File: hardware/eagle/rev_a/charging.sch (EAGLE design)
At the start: 25 parts, among them U1 LM2622

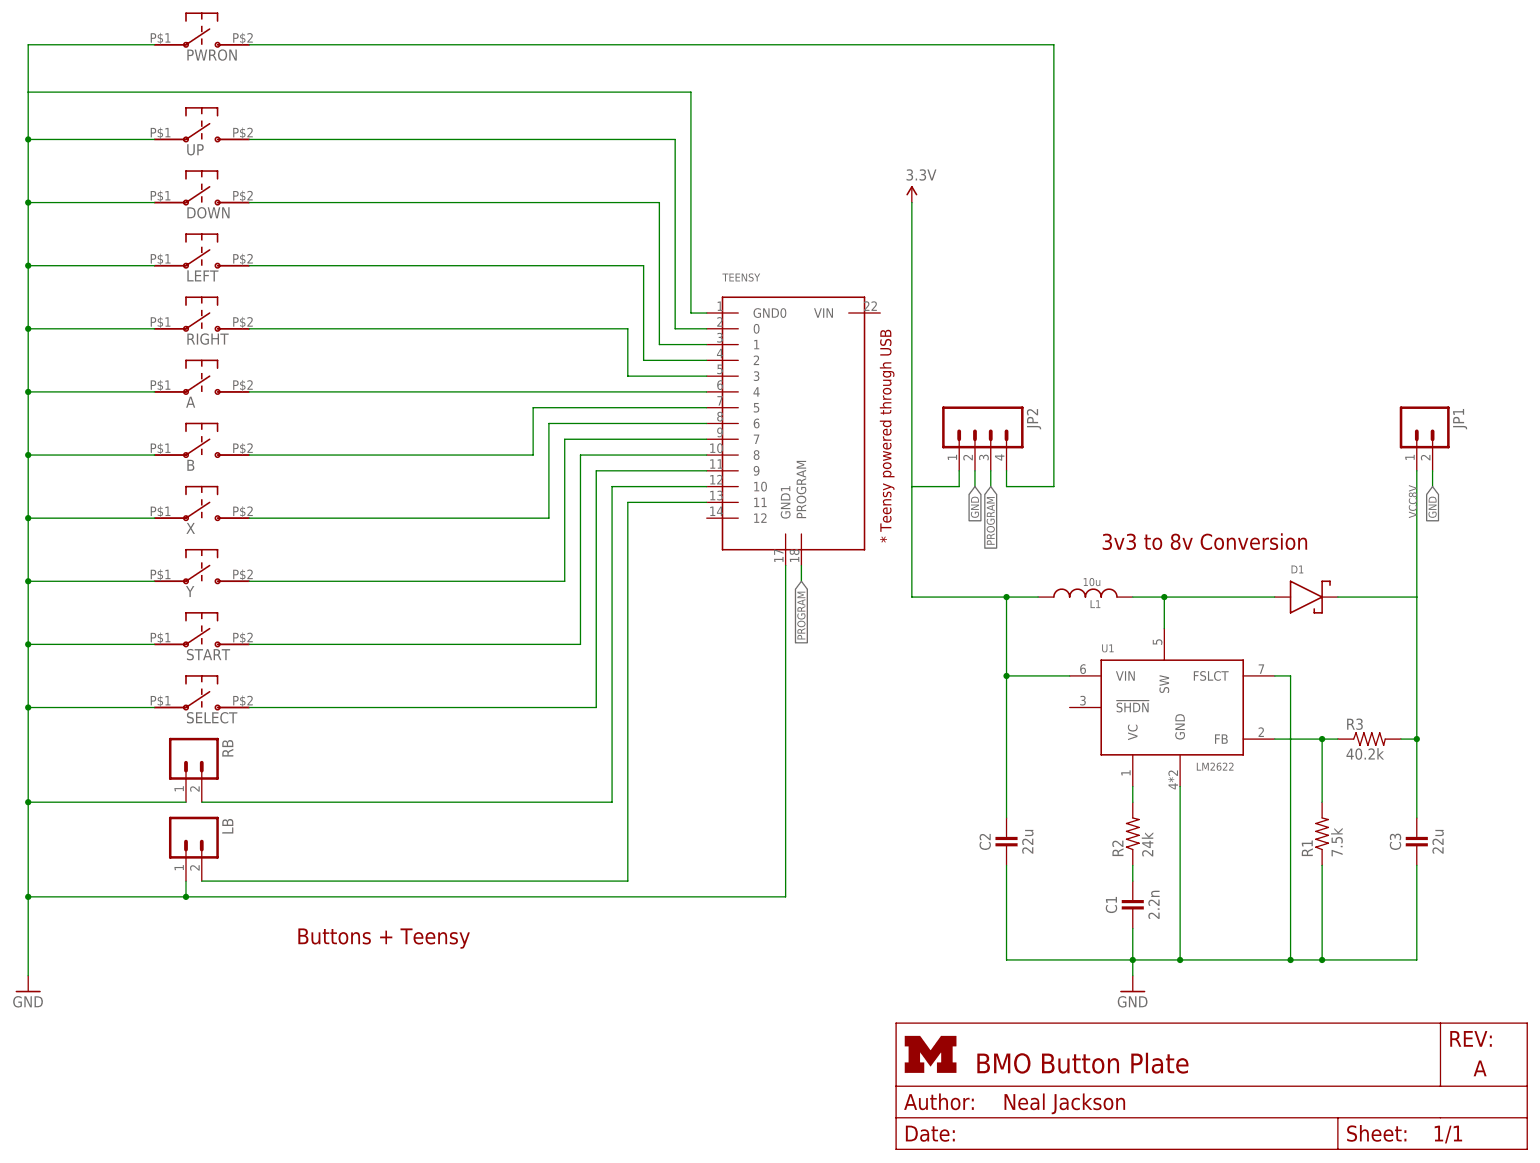
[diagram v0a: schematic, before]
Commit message: Added boards for back buttons and charging/serial port Tweaks and redesigns for button/usb boards to fit in case better
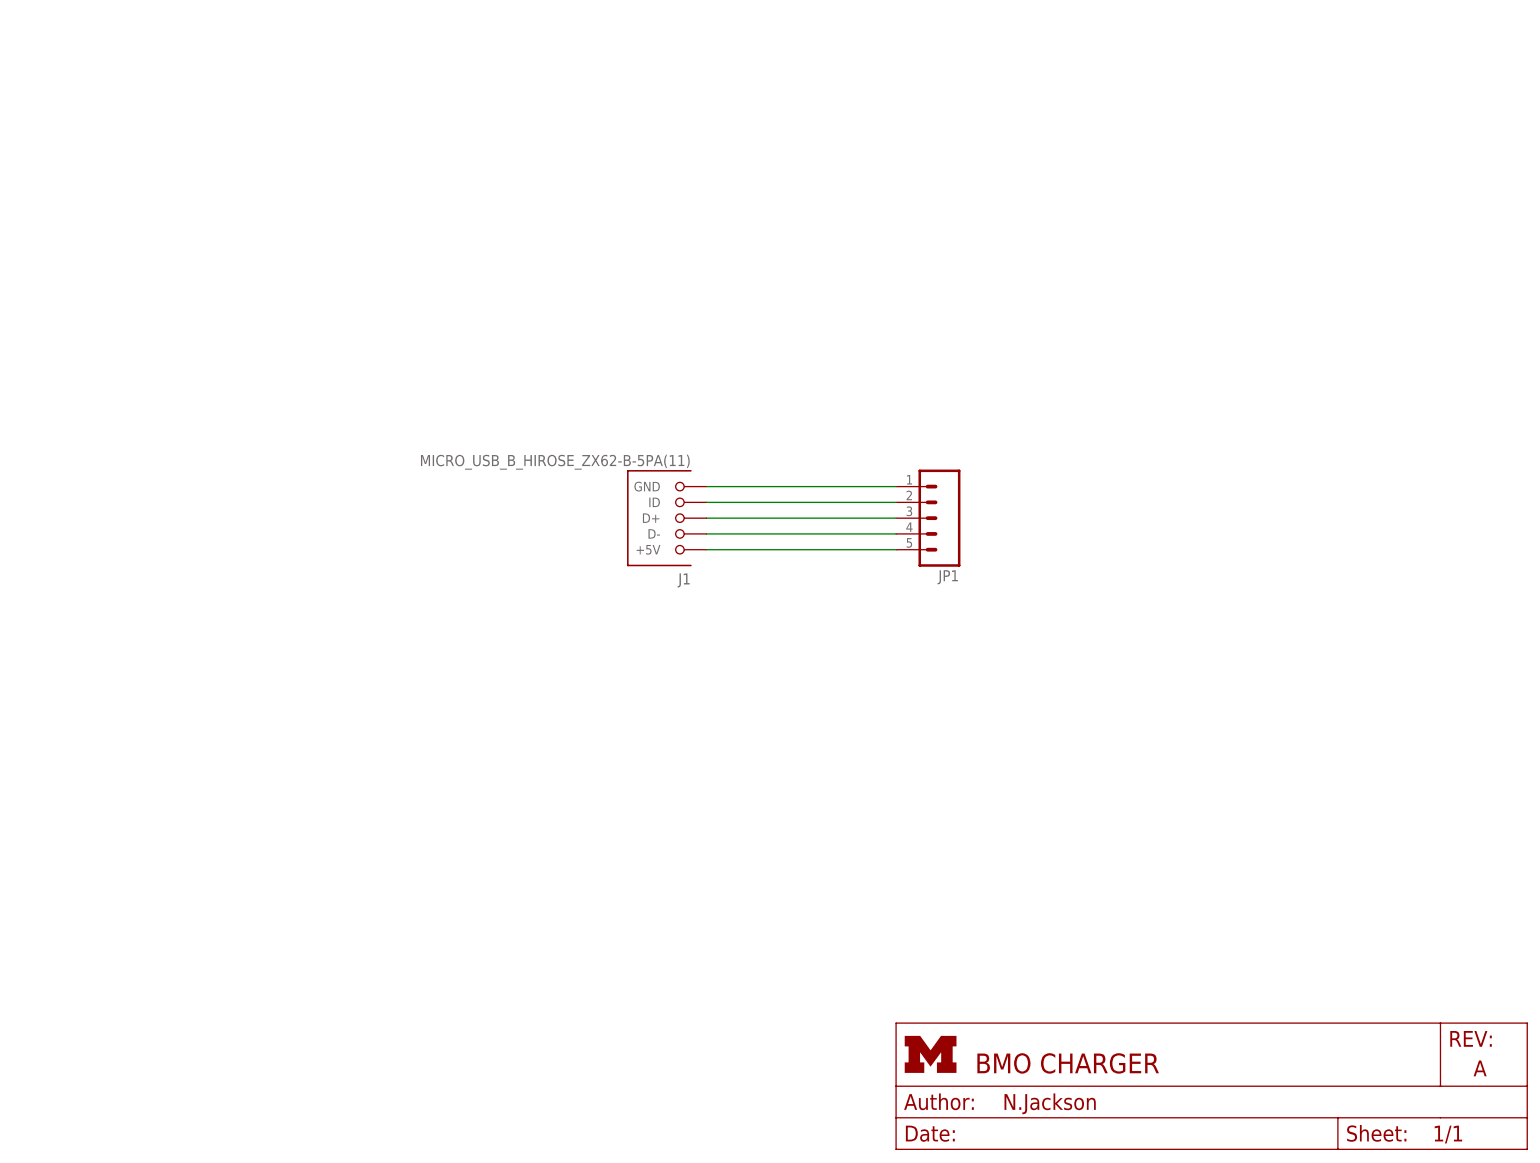
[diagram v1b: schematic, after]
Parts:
- removed A, B, DOWN, LEFT, PWRON, RIGHT, UP, X, Y: SKPDAMD010, switches:SKPDAMD010
- removed C1: 2.2n, passives:CAPACITOR
- removed C2, C3: 22u, passives:CAPACITOR
- removed D1: MBRM140T3G, BMO:MBRM140T3G
- removed JP2: (no value), SparkFun-Connectors:M04PTH
- removed L1: 10u, passives:INDUCTOR0402
- removed LB, RB: (no value), SparkFun-Connectors:M02PTH
- removed R1: 7.5k, passives:RESISTOR0402_RES
- removed R2: 24k, passives:RESISTOR0402_RES
- removed R3: 40.2k, passives:RESISTOR0402_RES
- removed SELECT, START: EVQ11D09K, BMO:EVQ11D09K
- removed TEENSY: TEENSY_LC, BMO:TEENSY_LC
- removed U1: LM2622, BMO:LM2622
- added J1: MICRO_USB_B_HIROSE_ZX62-B-5PA(11), connector:MICRO_USB_B_HIROSE_ZX62-B-5PA(11)
- JP1: device SparkFun-Connectors:M02PTH -> SparkFun-Connectors:M05PTH
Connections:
- removed net 3.3V: C2.1, JP2.1, L1.1, U1.VIN
- removed net N$1: A.P$2, TEENSY.4
- removed net N$10: TEENSY.7, Y.P$2
- removed net N$11: START.P$2, TEENSY.8
- removed net N$12: SELECT.P$2, TEENSY.9
- removed net N$13: RB.2, TEENSY.10
- removed net N$14: LB.2, TEENSY.11
- removed net N$15: R2.2, U1.VC
- removed net N$16: D1.ANODE, L1.2, U1.SW
- removed net N$17: R1.2, R3.1, U1.FB
- removed net N$2: JP2.4, PWRON.P$2
- removed net N$3: TEENSY.0, UP.P$2
- removed net N$4: DOWN.P$2, TEENSY.1
- removed net N$5: LEFT.P$2, TEENSY.2
- removed net N$6: RIGHT.P$2, TEENSY.3
- removed net N$7: C1.1, R2.1
- removed net N$8: B.P$2, TEENSY.5
- removed net N$9: TEENSY.6, X.P$2
- removed net PROGRAM: JP2.3, TEENSY.PROGRAM
- removed net VCC8V: C3.1, D1.CATHODE, JP1.1, R3.2
- new net 5V: J1.+5V, JP1.5
- new net D+: J1.D+, JP1.3
- new net D-: J1.D-, JP1.4
- new net ID: J1.ID, JP1.2
- net GND: now also J1.GND, JP1.1; no longer A.P$1, B.P$1, C1.2, C2.2, C3.2, DOWN.P$1, JP1.2, JP2.2, LB.1, LEFT.P$1, PWRON.P$1, R1.1, RB.1, RIGHT.P$1, SELECT.P$1, START.P$1, TEENSY.GND0, TEENSY.GND1, U1.FSLCT, U1.GND, UP.P$1, X.P$1, Y.P$1
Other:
- note removed: "* Teensy powered through USB"
- note removed: "3v3 to 8v Conversion"
- note removed: "Buttons + Teensy"
